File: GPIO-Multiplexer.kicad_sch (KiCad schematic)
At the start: 3 parts, among them U701 PCF8575DBR

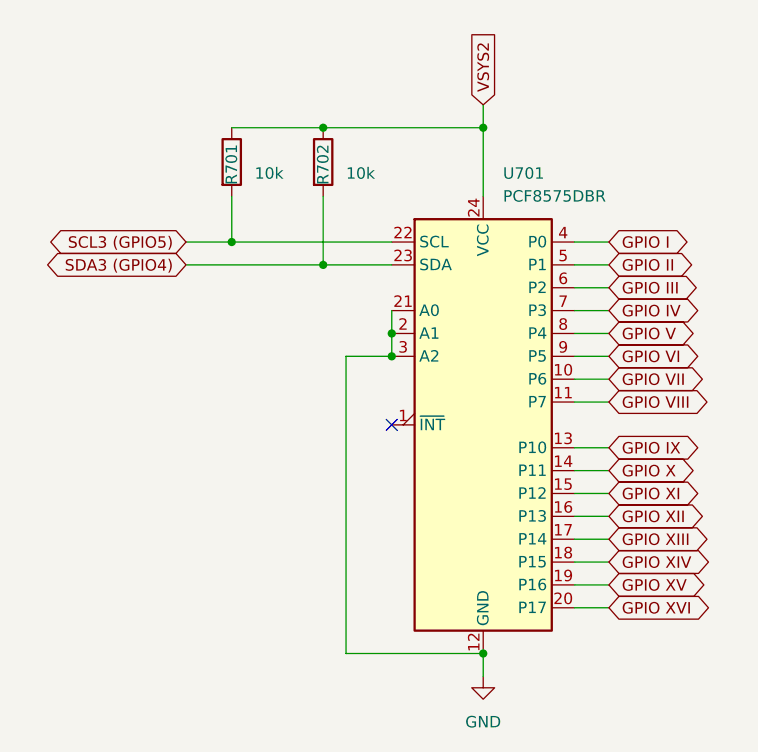
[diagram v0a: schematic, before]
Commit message: Add files via upload
cleaned up, board outline changed, cons cleaned up, 
GPIO now prepped for breakout board.
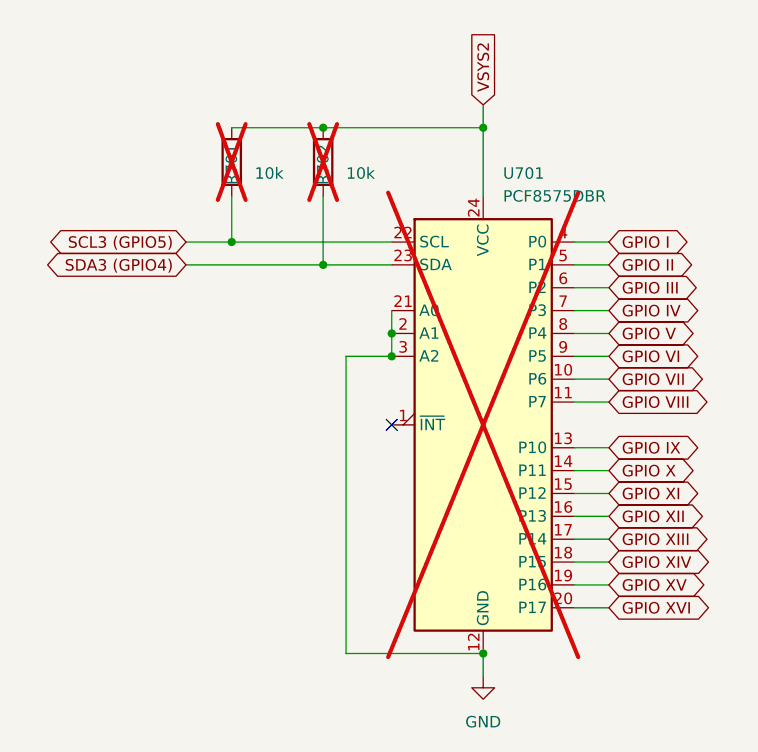
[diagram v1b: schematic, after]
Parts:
- R701, R702, U701: now not fitted
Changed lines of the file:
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@@
 		(exclude_from_sim no)
 		(in_bom yes)
-		(on_board yes)
-		(dnp no)
+		(on_board no)
+		(dnp yes)
 		(fields_autoplaced yes)
 		(property "Reference" "U701"
@@
 		(exclude_from_sim no)
 		(in_bom yes)
-		(on_board yes)
-		(dnp no)
+		(on_board no)
+		(dnp yes)
 		(property "Reference" "R702"
 			(at 60.96 53.34 90)
@@
 		(exclude_from_sim no)
 		(in_bom yes)
-		(on_board yes)
-		(dnp no)
+		(on_board no)
+		(dnp yes)
 		(property "Reference" "R701"
 			(at 50.8 53.34 90)

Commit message: daughterboard created
divided into mainboard and daughterboard
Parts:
- removed R701, R702: 10k, Resistor_SMD:R_0402_1005Metric, symbol Device:R
- removed U701: PCF8575DBR, PFC8575CRGER:RGE24_2P1X2P1, symbol Interface_Expansion:PCF8575DBR
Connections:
- no-connect marks 1 -> 0
